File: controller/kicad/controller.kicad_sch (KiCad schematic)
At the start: 27 parts, among them J1 pcie_98, U1 WeAct_STM32H750_Module, U10 ESD5344D, U11 ESD5344D, U12 ESD5344D, U13 ESD5344D, U14 ESD5344D, U15 ESD5344D, U16 ESD5344D, U17 ESD5344D, U18 ESD5344D, U19 ESD5344D, U2 ESD5344D, U20 ESD5344D, U21 ESD5344D, U3 ESD5344D, U4 ESD5344D, U5 ESD5344D, U6 ESD5344D, U7 ESD5344D, U8 ESD5344D, U9 ESD5344D

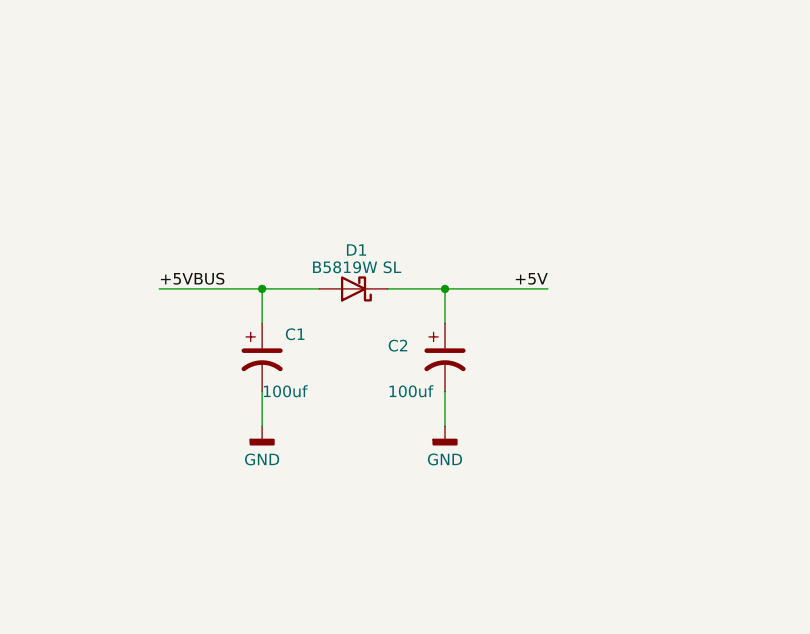
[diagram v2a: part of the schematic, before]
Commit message: Added Controller doc and added an optional jumper to short the Schottky diode.
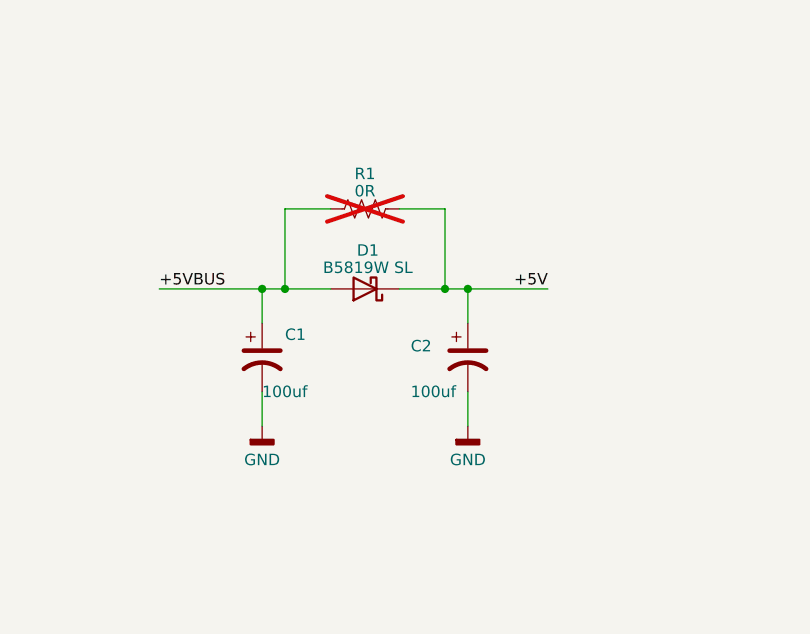
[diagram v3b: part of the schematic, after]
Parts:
- added R1: 0R, Resistor_SMD:R_0805_2012Metric, symbol Device:R_US
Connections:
- net +5V: now also R1.2
- net +5VBUS: now also R1.1
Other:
- moved on the sheet: C2, D1
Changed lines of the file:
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@@
   (junction (at 105.41 45.72) (diameter 0) (color 0 0 0 0)
   )
+  (junction (at 186.69 73.66) (diameter 0) (color 0 0 0 0)
+  )
   (junction (at 184.15 73.66) (diameter 0) (color 0 0 0 0)
   )
@@
   (junction (at 83.82 50.8) (diameter 0) (color 0 0 0 0)
   )
+  (junction (at 166.37 73.66) (diameter 0) (color 0 0 0 0)
+  )
   (junction (at 83.82 48.26) (diameter 0) (color 0 0 0 0)
   )
@@
     (stroke (width 0) (type default))
   )
+  (wire (pts (xy 166.37 73.66) (xy 171.45 73.66))
+    (stroke (width 0) (type default))
+  )
   (wire (pts (xy 240.03 63.5) (xy 250.19 63.5))
     (stroke (width 0) (type default))
@@
     (stroke (width 0) (type default))
   )
-  (wire (pts (xy 177.8 73.66) (xy 184.15 73.66))
+  (wire (pts (xy 179.07 73.66) (xy 184.15 73.66))
     (stroke (width 0) (type default))
   )
@@
     (stroke (width 0) (type default))
   )
-  (wire (pts (xy 184.15 73.66) (xy 184.15 77.47))
+  (wire (pts (xy 186.69 73.66) (xy 186.69 77.47))
     (stroke (width 0) (type default))
   )
@@
     (stroke (width 0) (type default))
   )
-  (wire (pts (xy 184.15 73.66) (xy 195.58 73.66))
+  (wire (pts (xy 186.69 73.66) (xy 195.58 73.66))
     (stroke (width 0) (type default))
   )
@@
     (stroke (width 0) (type default))
   )
-  (wire (pts (xy 184.15 85.09) (xy 184.15 88.9))
+  (wire (pts (xy 186.69 85.09) (xy 186.69 88.9))
     (stroke (width 0) (type default))
   )
@@
     (stroke (width 0) (type default))
   )
+  (wire (pts (xy 184.15 73.66) (xy 186.69 73.66))
+    (stroke (width 0) (type default))
+  )
   (wire (pts (xy 198.12 208.28) (xy 203.2 208.28))
     (stroke (width 0) (type default))
@@
     (stroke (width 0) (type default))
   )
+  (wire (pts (xy 166.37 64.77) (xy 166.37 73.66))
+    (stroke (width 0) (type default))
+  )
   (wire (pts (xy 321.31 66.04) (xy 311.15 66.04))
     (stroke (width 0) (type default))
@@
     (stroke (width 0) (type default))
   )
+  (wire (pts (xy 179.07 64.77) (xy 184.15 64.77))
+    (stroke (width 0) (type default))
+  )
   (wire (pts (xy 275.59 63.5) (xy 285.75 63.5))
     (stroke (width 0) (type default))
@@
     (stroke (width 0) (type default))
   )
+  (wire (pts (xy 171.45 64.77) (xy 166.37 64.77))
+    (stroke (width 0) (type default))
+  )
   (wire (pts (xy 275.59 106.68) (xy 285.75 106.68))
     (stroke (width 0) (type default))
@@
     (stroke (width 0) (type default))
   )
-  (wire (pts (xy 163.83 73.66) (xy 170.18 73.66))
+  (wire (pts (xy 163.83 73.66) (xy 166.37 73.66))
     (stroke (width 0) (type default))
   )
@@
     (stroke (width 0) (type default))
   )
+  (wire (pts (xy 184.15 64.77) (xy 184.15 73.66))
+    (stroke (width 0) (type default))
+  )
   (wire (pts (xy 275.59 83.82) (xy 285.75 83.82))
     (stroke (width 0) (type default))
@@
     )
   )
-  (symbol (lib_id "Device:D_Schottky") (at 173.99 73.66 180) (unit 1)
+  (symbol (lib_id "Device:D_Schottky") (at 175.26 73.66 180) (unit 1)
     (in_bom yes) (on_board yes) (dnp no) (fields_autoplaced)
-    (property "Reference" "D1" (at 174.3075 69.3801 0)
+    (property "Reference" "D1" (at 175.5775 69.3801 0)
       (effects (font (size 1.27 1.27)))
     )
-    (property "Value" "B5819W SL" (at 174.3075 71.3011 0)
+    (property "Value" "B5819W SL" (at 175.5775 71.3011 0)
       (effects (font (size 1.27 1.27)))
     )
-    (property "Footprint" "Diode_SMD:D_SOD-123" (at 173.99 73.66 0)
+    (property "Footprint" "Diode_SMD:D_SOD-123" (at 175.26 73.66 0)
       (effects (font (size 1.27 1.27)) hide)
     )
-    (property "Datasheet" "https://datasheet.lcsc.com/lcsc/1809140216_Jiangsu-Changjing-Electronics-Technology-Co---Ltd--B5819W-SL_C8598.pdf" (at 173.99 73.66 0)
+    (property "Datasheet" "https://datasheet.lcsc.com/lcsc/1809140216_Jiangsu-Changjing-Electronics-Technology-Co---Ltd--B5819W-SL_C8598.pdf" (at 175.26 73.66 0)
       (effects (font (size 1.27 1.27)) hide)
     )
-    (property "LCSC" "C8598" (at 173.99 73.66 0)
+    (property "LCSC" "C8598" (at 175.26 73.66 0)
       (effects (font (size 1.27 1.27)) hide)
     )
@@
     )
   )
-  (symbol (lib_id "controller:GND") (at 184.15 88.9 0) (unit 1)
+  (symbol (lib_id "controller:GND") (at 186.69 88.9 0) (unit 1)
     (in_bom yes) (on_board yes) (dnp no) (fields_autoplaced)
-    (property "Reference" "#PWR03" (at 184.15 95.25 0)
+    (property "Reference" "#PWR03" (at 186.69 95.25 0)
       (effects (font (size 1.27 1.27)) hide)
     )
-    (property "Value" "GND" (at 184.15 92.6545 0)
+    (property "Value" "GND" (at 186.69 92.6545 0)
       (effects (font (size 1.27 1.27)))
     )
-    (property "Footprint" "" (at 184.15 88.9 0)
+    (property "Footprint" "" (at 186.69 88.9 0)
       (effects (font (size 1.27 1.27)) hide)
     )
-    (property "Datasheet" "" (at 184.15 88.9 0)
+    (property "Datasheet" "" (at 186.69 88.9 0)
       (effects (font (size 1.27 1.27)) hide)
     )
@@
     )
   )
+  (symbol (lib_id "Device:R_US") (at 175.26 64.77 90) (unit 1)
+    (in_bom no) (on_board yes) (dnp yes) (fields_autoplaced)
+    (property "Reference" "R1" (at 175.26 60.8711 90)
+      (effects (font (size 1.27 1.27)))
+    )
+    (property "Value" "0R" (at 175.26 62.7921 90)
+      (effects (font (size 1.27 1.27)))
+    )
+    (property "Footprint" "Resistor_SMD:R_0805_2012Metric" (at 175.514 63.754 90)
+      (effects (font (size 1.27 1.27)) hide)
+    )
+    (property "Datasheet" "~" (at 175.26 64.77 0)
+      (effects (font (size 1.27 1.27)) hide)
+    )
+    (property "LCSC" "C17477" (at 175.26 64.77 90)
+      (effects (font (size 1.27 1.27)) hide)
+    )
+    (pin "1")
+    (pin "2")
+    (instances
+      (project "controller"
+        (path "/0dcd9c8c-bd5a-437f-856e-101fb6cf8b66"
+          (reference "R1") (unit 1)
+        )
+      )
+    )
+  )
   (symbol (lib_id "controller:GND") (at 364.49 68.58 0) (unit 1)
     (in_bom yes) (on_board yes) (dnp no) (fields_autoplaced)
@@
     )
   )
-  (symbol (lib_id "Device:C_Polarized_US") (at 184.15 81.28 0) (unit 1)
+  (symbol (lib_id "Device:C_Polarized_US") (at 186.69 81.28 0) (unit 1)
     (in_bom yes) (on_board yes) (dnp no)
-    (property "Reference" "C2" (at 177.8 80.01 0)
+    (property "Reference" "C2" (at 180.34 80.01 0)
       (effects (font (size 1.27 1.27)) (justify left))
     )
-    (property "Value" "100uf" (at 177.8 85.09 0)
+    (property "Value" "100uf" (at 180.34 85.09 0)
       (effects (font (size 1.27 1.27)) (justify left))
     )
-    (property "Footprint" "Capacitor_SMD:CP_Elec_5x5.4" (at 184.15 81.28 0)
+    (property "Footprint" "Capacitor_SMD:CP_Elec_5x5.4" (at 186.69 81.28 0)
       (effects (font (size 1.27 1.27)) hide)
     )
-    (property "Datasheet" "https://datasheet.lcsc.com/lcsc/2202252030_ROQANG-RVE1A101M0505_C131115.pdf" (at 184.15 81.28 0)
+    (property "Datasheet" "https://datasheet.lcsc.com/lcsc/2202252030_ROQANG-RVE1A101M0505_C131115.pdf" (at 186.69 81.28 0)
       (effects (font (size 1.27 1.27)) hide)
     )
-    (property "LCSC" "C131115" (at 184.15 81.28 0)
+    (property "LCSC" "C131115" (at 186.69 81.28 0)
       (effects (font (size 1.27 1.27)) hide)
     )

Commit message: Fixed the orientation of the 100uf capacitors for JLCPCB.
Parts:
- C1, C2: footprint Capacitor_SMD:CP_Elec_5x5.4 -> controller:CP_Elec_5x5.4_JLCPCB
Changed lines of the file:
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@@
       (effects (font (size 1.27 1.27)) (justify left))
     )
-    (property "Footprint" "Capacitor_SMD:CP_Elec_5x5.4" (at 163.83 81.28 0)
+    (property "Footprint" "controller:CP_Elec_5x5.4_JLCPCB" (at 163.83 81.28 0)
       (effects (font (size 1.27 1.27)) hide)
     )
@@
       (effects (font (size 1.27 1.27)) (justify left))
     )
-    (property "Footprint" "Capacitor_SMD:CP_Elec_5x5.4" (at 186.69 81.28 0)
-      (effects (font (size 1.27 1.27)) hide)
-    )
+    (property "Footprint" "controller:CP_Elec_5x5.4_JLCPCB" (at 186.69 81.28 0)
+      (effects (font (size 1.27 1.27)) hide)
+    )

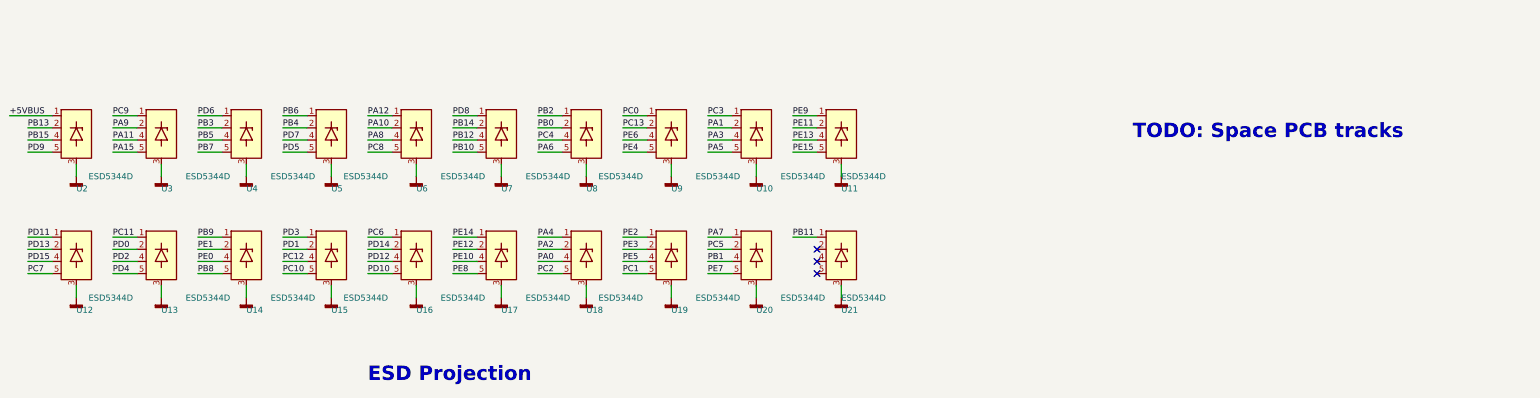
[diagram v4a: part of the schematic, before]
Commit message: Spaced the PCB traks.
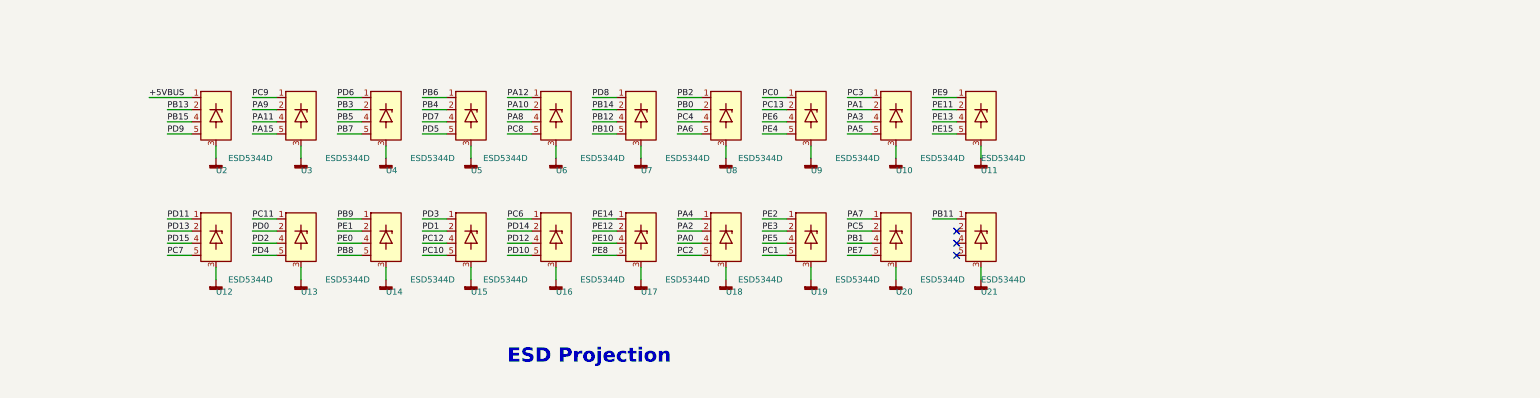
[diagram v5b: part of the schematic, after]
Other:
- note removed: "TODO: Space PCB tracks"
- moved on the sheet: U10, U11, U12, U13, U14, U15, U16, U17, U18, U19, U2, U20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

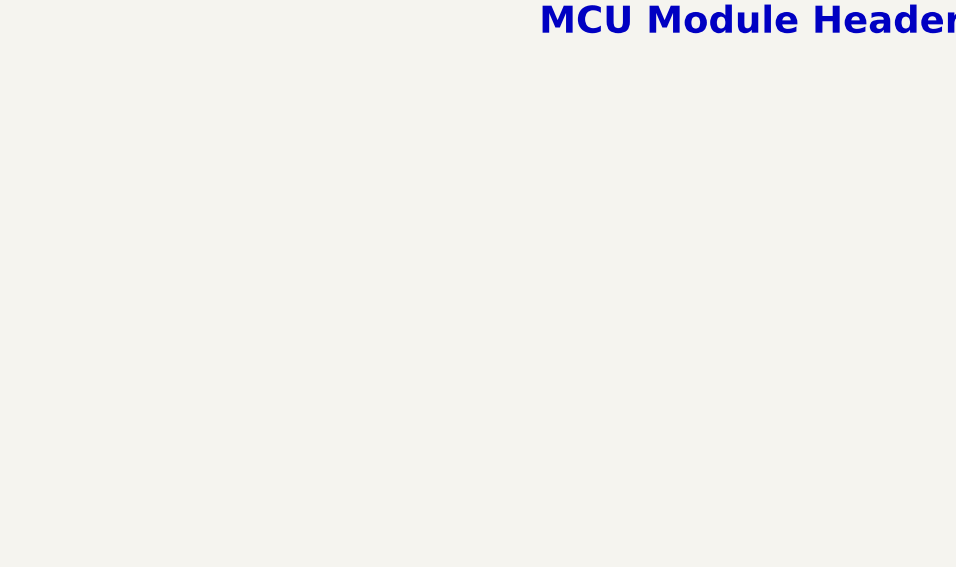
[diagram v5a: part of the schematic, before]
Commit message: Added TODO comments.
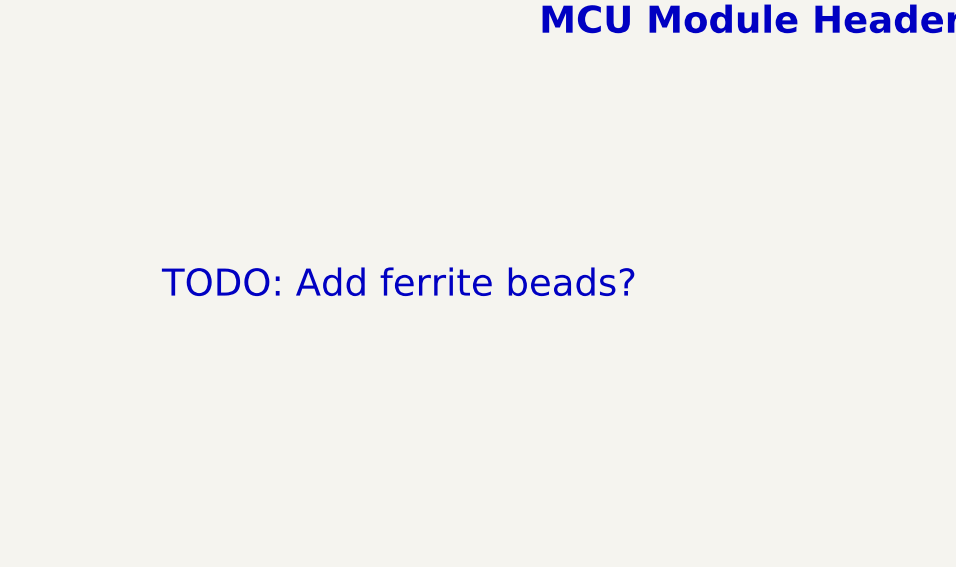
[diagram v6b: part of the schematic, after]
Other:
- note added: "TODO: Add ferrite beads?"
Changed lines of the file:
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@@
     (effects (font (size 3 3) (thickness 0.6) bold) (justify left bottom))
+  )
+  (text "TODO: Add ferrite beads?" (at 238.76 163.83 0)
+    (effects (font (size 3 3) (color 255 0 0 1)) (justify left bottom))
   )
   (text "MCU Module Headers" (at 280.67 134.62 0)

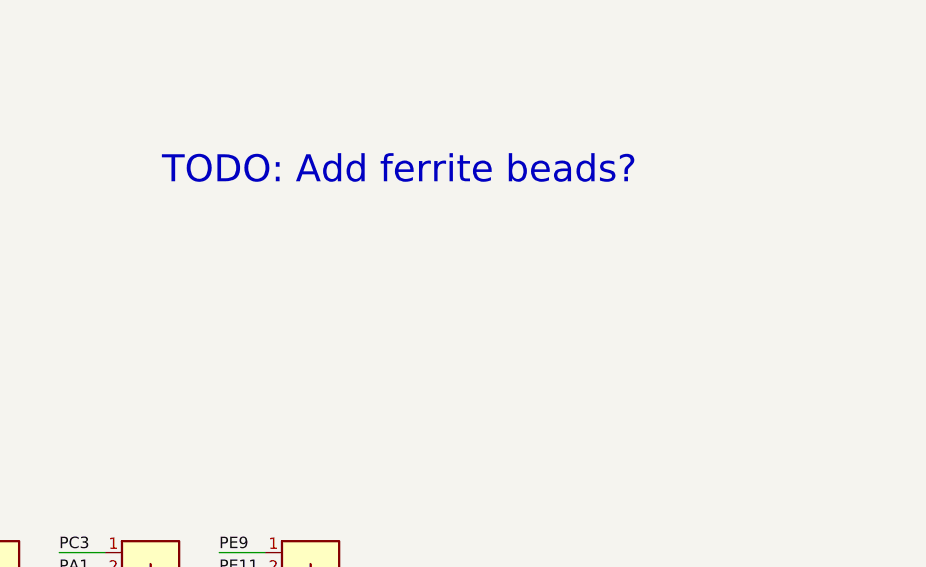
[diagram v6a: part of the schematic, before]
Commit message: Added LEDs, test points, and LCSC ids.
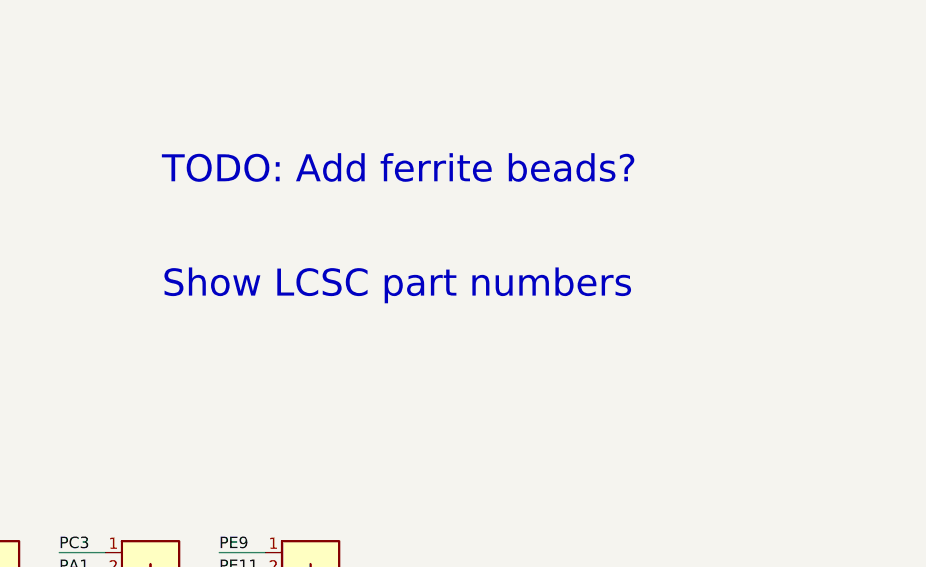
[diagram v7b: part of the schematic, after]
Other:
- note added: "Show LCSC part numbers"
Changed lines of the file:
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@@
     (effects (font (size 3 3) (thickness 0.6) bold) (justify left bottom))
+  )
+  (text "Show LCSC part numbers" (at 238.76 176.53 0)
+    (effects (font (size 3 3) (color 255 0 0 1)) (justify left bottom))
   )
   (text "TODO: Add ferrite beads?" (at 238.76 163.83 0)
